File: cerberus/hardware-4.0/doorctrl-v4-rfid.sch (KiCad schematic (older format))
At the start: 19 parts, among them Q1 BC817, Q2 BC807, U1 LM358

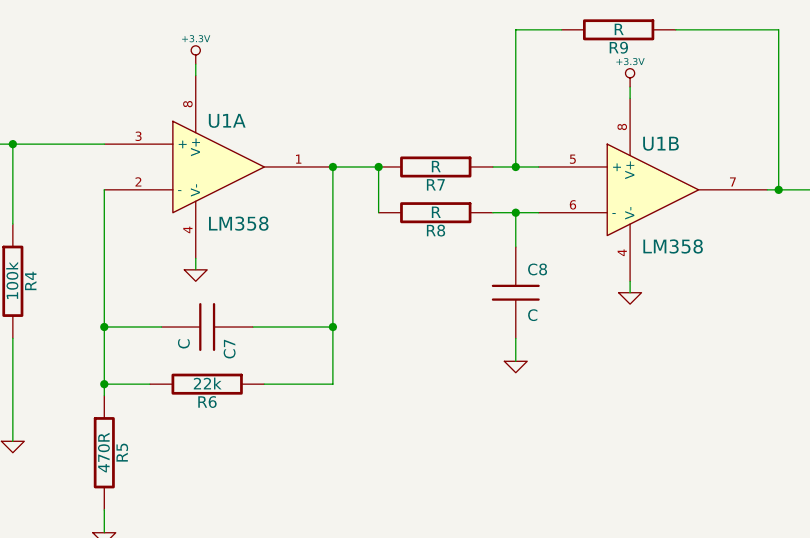
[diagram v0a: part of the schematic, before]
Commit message: Tried converting the rj45 connector
git-svn-id: file:///home/ff/projects/osaa/svn@206 a092026d-3e22-4cff-94a7-eaa6fdd35d37
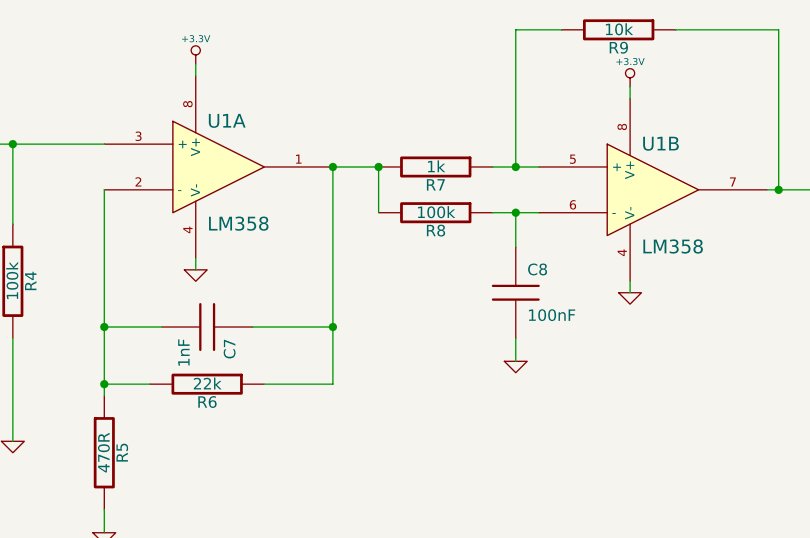
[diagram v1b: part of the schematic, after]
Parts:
- C7: value C -> 1nF
- C8: value C -> 100nF
- R7: value R -> 1k
- R8: value R -> 100k
- R9: value R -> 10k
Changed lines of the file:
@@
-EESchema Schematic File Version 2  date 2010-12-06T22:12:19 CET
+EESchema Schematic File Version 2  date 2010-12-07T16:59:15 CET
 LIBS:power
 LIBS:device
@@
 LIBS:bc807
 LIBS:bc817
-LIBS:doorctrl-v4-cache
 EELAYER 24  0
 EELAYER END
@@
 Sheet 4 6
 Title ""
-Date "6 dec 2010"
+Date "7 dec 2010"
 Rev ""
 Comp ""
@@
 P 7300 3700
 F 0 "C7" H 7350 3800 50  0000 L CNN
-F 1 "C" H 7350 3600 50  0000 L CNN
+F 1 "1nF" H 7350 3600 50  0000 L CNN
 	1    7300 3700
 	0    1    1    0
@@
 P 8650 3550
 F 0 "C8" H 8700 3650 50  0000 L CNN
-F 1 "C" H 8700 3450 50  0000 L CNN
+F 1 "100nF" H 8700 3450 50  0000 L CNN
 	1    8650 3550
 	1    0    0    -1
@@
 P 8300 3200
 F 0 "R8" V 8380 3200 50  0000 C CNN
-F 1 "R" V 8300 3200 50  0000 C CNN
+F 1 "100k" V 8300 3200 50  0000 C CNN
 	1    8300 3200
 	0    1    1    0
@@
 P 8300 3000
 F 0 "R7" V 8380 3000 50  0000 C CNN
-F 1 "R" V 8300 3000 50  0000 C CNN
+F 1 "1k" V 8300 3000 50  0000 C CNN
 	1    8300 3000
 	0    1    1    0
@@
 P 9100 2400
 F 0 "R9" V 9180 2400 50  0000 C CNN
-F 1 "R" V 9100 2400 50  0000 C CNN
+F 1 "10k" V 9100 2400 50  0000 C CNN
 	1    9100 2400
 	0    1    1    0
